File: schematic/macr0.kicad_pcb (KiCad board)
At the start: 2 copper layers, 43.2 x 43.2 mm, 25 parts, among them J1 USB-C, J2 ISP, U1 ATmega32U4, U2 CAT4104, Y1 16MHz

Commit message: First prototype pcb for fab.
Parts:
- moved C1 155.1 mm to (123.7, 96.2)
- moved C2 155.1 mm to (125.2, 103.6)
- moved C3 155.1 mm to (131.6, 113.1)
- moved C4 155.1 mm to (132.4, 108.1)
- moved D1 155.1 mm to (122.8, 81.4)
- moved D2 155.1 mm to (151.0, 81.4)
- moved D3 155.1 mm to (125.0, 100.5)
- moved D4 155.1 mm to (150.4, 99.8)
- moved J1 155.1 mm to (136.4, 83.3)
- moved J2 155.1 mm to (138.4, 111.5)
- moved R1 155.1 mm to (142.0, 115.1)
- moved R2 155.1 mm to (151.4, 97.3)
- moved R3 155.1 mm to (132.4, 92.0)
- moved R4 155.1 mm to (142.3, 92.4)
- moved R5 155.1 mm to (127.9, 81.4)
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
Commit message: Added logo to pcb.  Created readme.
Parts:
- added G***: LOGO, macr0:clewsy_logo_8mm, B.Cu at (121.2, 114.0)
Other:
- board text added: "clewsy.pro"

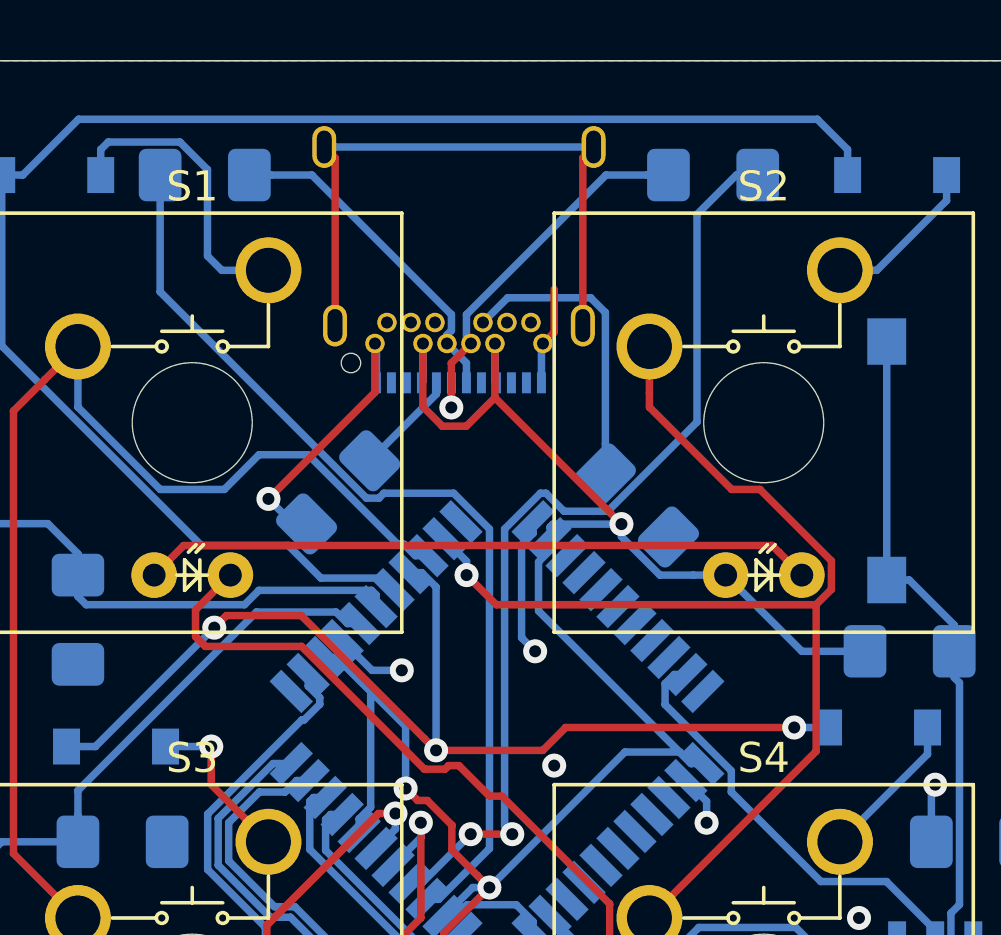
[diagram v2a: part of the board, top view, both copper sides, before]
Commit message: USB receptacle was a deprecated part but I found a better one intended for USB 2.0 devices.
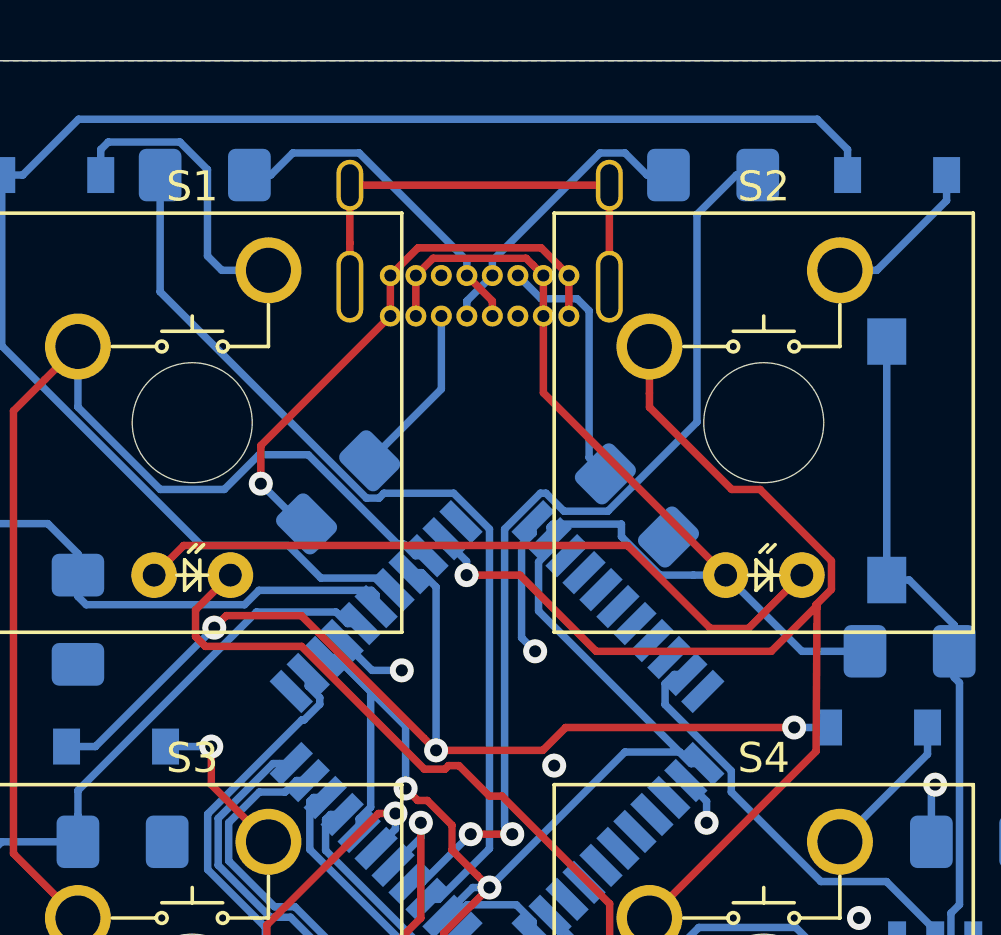
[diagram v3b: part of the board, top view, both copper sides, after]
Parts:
- D1, D2, D3, D4: value 4148 -> 1N4148
- J1: footprint Connector_USB:USB_C_Receptacle_Amphenol_12401548E4-2A -> Connector_USB:USB_C_Receptacle_GCT_USB4085
- J2: value ISP -> AVR-ISP-6
- S0: value DIMMER -> BRIGHTNESS
- U1: value ATmega32U4 -> ATmega32U4-AU
- moved J1 3.61 mm to (134.1, 86.1)
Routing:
- net GND: track 43.5 -> 49.4 mm
- net Net-(J1-PadS1): track 21.2 -> 15.4 mm
- net Net-(J1-PadA6): track 12.9 -> 9.86 mm, vias 1 -> 0
- net +5V: track 105.5 -> 108.5 mm, vias 4 -> 3
- net Net-(J1-PadA5): track 3.52 -> 5.82 mm
- net Net-(J1-PadB5): track 10.0 -> 8.52 mm
- net Net-(S1-Pad4): track 22.4 -> 23.9 mm
- net COL2: track 38.2 -> 39.5 mm
